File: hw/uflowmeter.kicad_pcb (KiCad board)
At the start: 4 copper layers, 70 x 55 mm, 54 parts, among them J1 SBW, J2 ANT, J3 Display, J4 Transducers, J5 Cal UART, Q1 IRLML6401, SW1 Button, U1 MSP430FR5043IRGC, U2 CC1101RGPR, Y1 32.768kHz, Y2 8MHz, Y3 26MHz

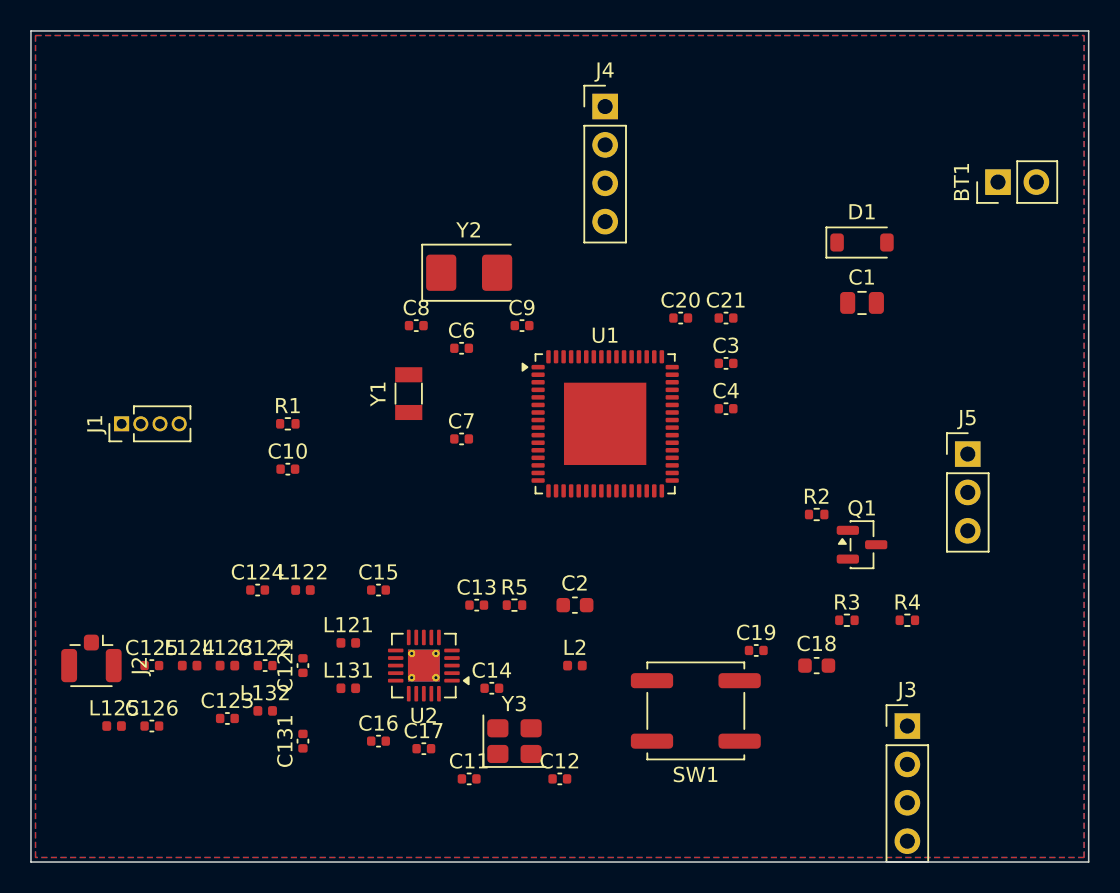
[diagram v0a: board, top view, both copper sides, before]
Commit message: hw: pour the planes and stitch the supplies, 134 unconnected down to 69
Ground and the supply rails are now carried by the planes rather than left to
routing, which is what a four-layer board is for. Filling the pours took the
unconnected count from 134 to 86; sixteen stitching vias taking VCC's surface
pads down to its plane took it to 70. DRC stays at zero violations.

The zones connect to pads solidly rather than through thermal spokes. With
relief, DRC reported starved thermals on the CC1101's ground pads -- a QFN at
0.5 mm pitch has no room for spokes -- and thermal relief under an RF ground
is the wrong thing anyway.

Signal routing is not done, and the attempt is worth recording. Straight runs
between pads were tried for the simple two-pad nets and refused themselves:
ten of eleven were blocked, because a straight line from a crystal to its QFN
pin passes over the neighbouring pins. Escaping the package and changing layer
is a router's job or a person's, not a script's.

The RF chain was excluded from that attempt on purpose. Its geometry has to be
lifted from TI's reference layout, and a generic trace between those pads
would be worse than none, because it would look finished.

Co-Authored-By: Claude Opus 5 (1M context) <noreply@anthropic.com>
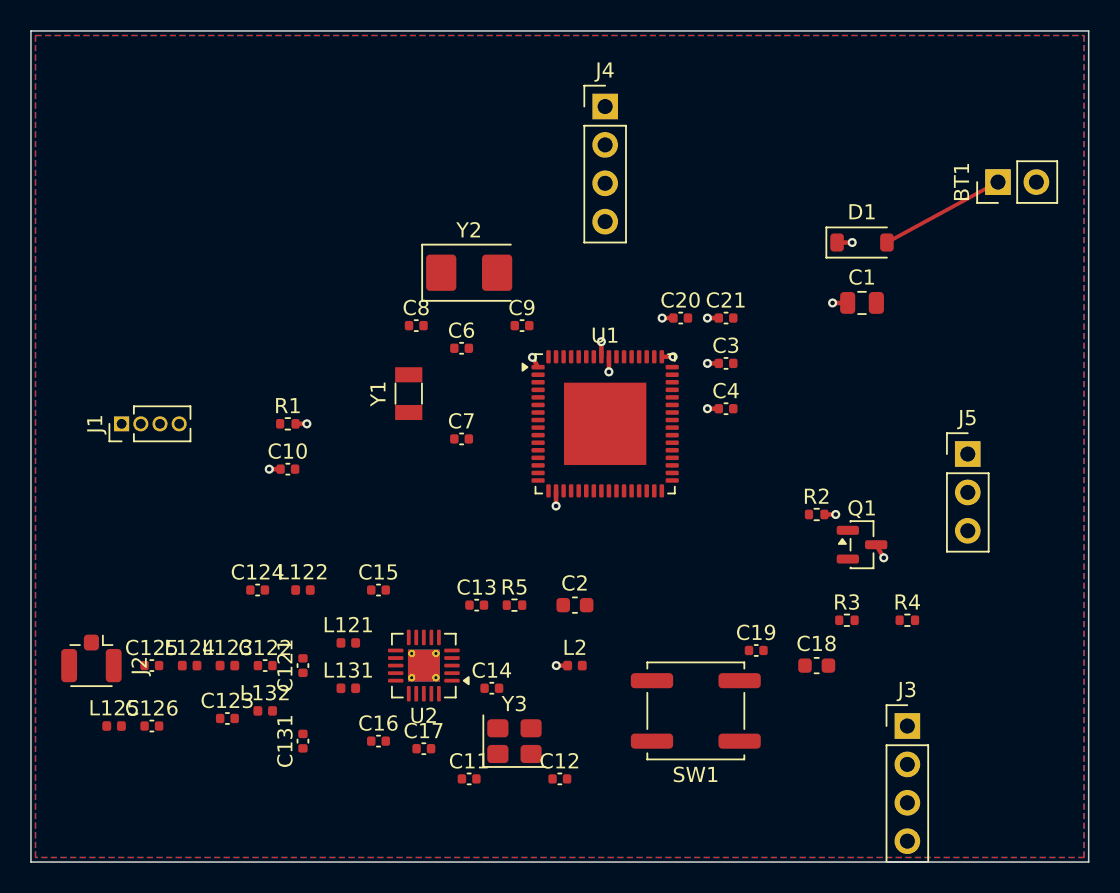
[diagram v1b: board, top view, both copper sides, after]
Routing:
- net VCC: track 0.00 -> 13.5 mm, vias 0 -> 16
- net BAT+: track 0.00 -> 8.37 mm

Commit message: hw: J3 is GND VCC SCL SDA, the way the module is actually labelled
The display header had VCC on pin 1 and ground on pin 2. The module in hand
is silkscreened GND VCC SCL SDA, so plugging it in would have put the supply
across it backwards the first time.

Both orders exist on SSD1306 breakouts, which is why this is now recorded as
having been read off the part rather than assumed -- it is worth checking
against the module in hand and not against habit.

DRC stays clean at 69 unconnected.

Co-Authored-By: Claude Opus 5 (1M context) <noreply@anthropic.com>
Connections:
- J3 pad 1: VCC_DISP -> GND
- J3 pad 2: GND -> VCC_DISP

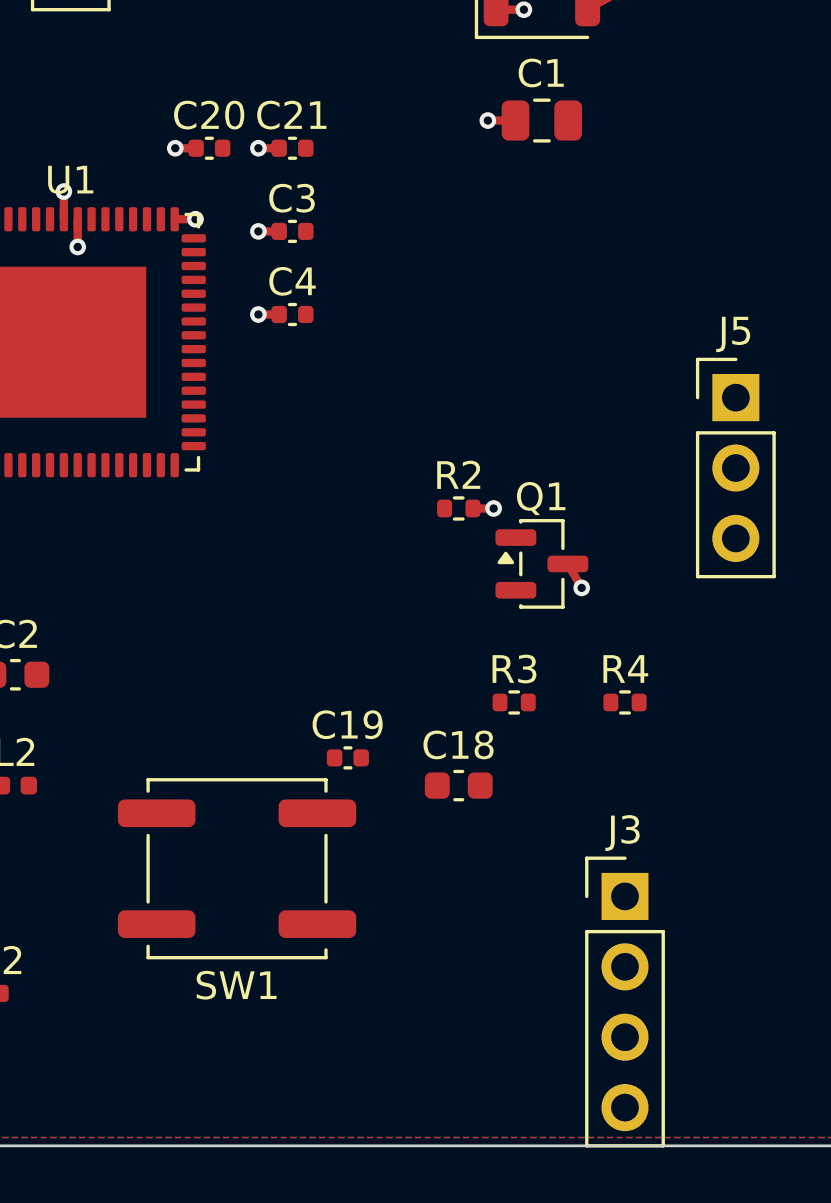
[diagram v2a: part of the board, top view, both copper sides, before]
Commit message: hw: the display mounts on the back of the board
J3 moves to the reverse side with its pins in a row rather than a column, so
the module seats directly on it facing outward instead of hanging on four
flying leads.

Where it sits was searched rather than chosen. Three constraints, and each
one rejected the position picked before it. The four drills have to miss
everything on the front -- the first attempt put them through the 8 MHz
crystal. The pin row has to run the way the module's does, or the display
reads sideways. And the 27 mm body has to clear every through-hole pin that
protrudes on that side, which J1, J4, J5 and BT1 all do; the position before
this one would have sat the module on top of the calibration header.

It also stays off the radio. A module carrying its own ground plane and a
charge pump, held a few millimetres over the 868 MHz balun, would detune the
match and inject noise into it.

Thirty-seven positions satisfy all of that. Pin 1 is at (43.5, 20.5) and the
body lands at x 33.8-60.8, y 20.5-47.5. DRC clean, 69 unconnected.

One thing to check with the part in hand: a header on the back reads mirrored
from the front, so which way round the module seats depends on which side its
body hangs.

Co-Authored-By: Claude Opus 5 (1M context) <noreply@anthropic.com>
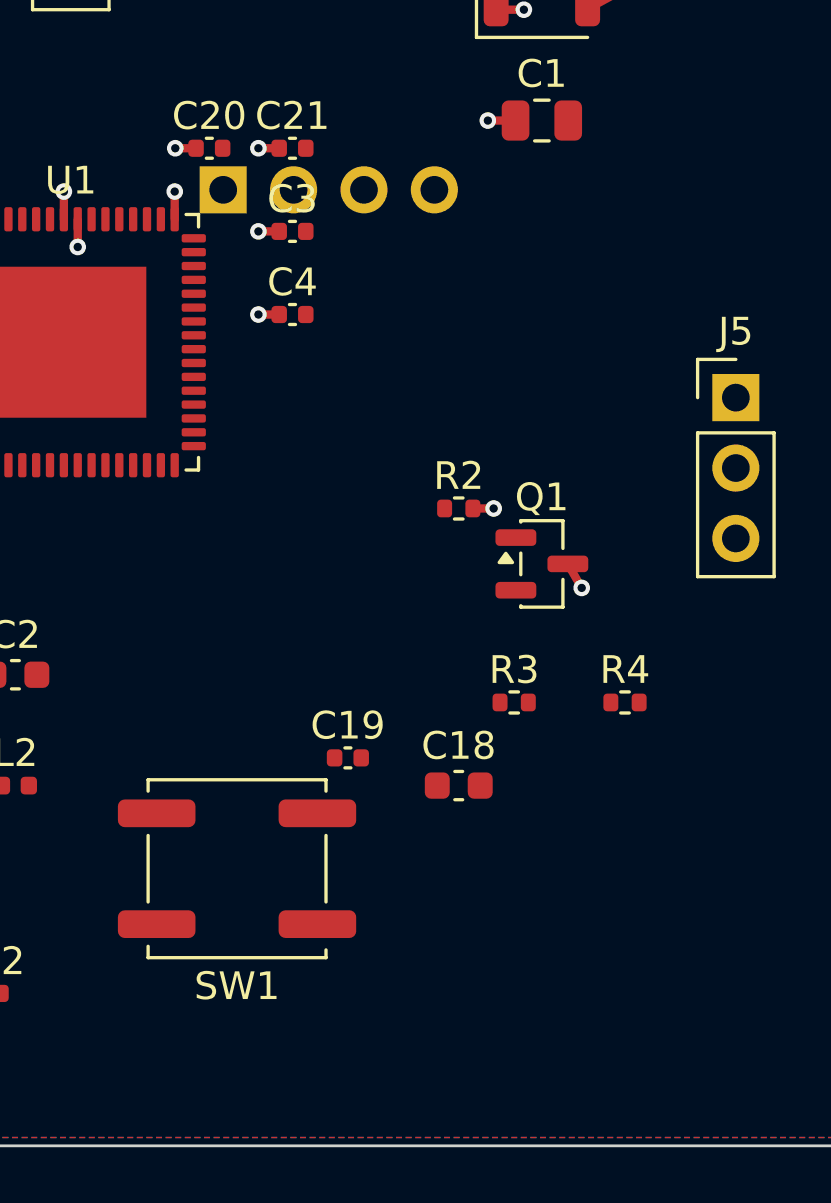
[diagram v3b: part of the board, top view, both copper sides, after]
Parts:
- J3: moved to B.Cu
- moved J3 29.3 mm to (43.5, 20.5), turned to -90 degrees

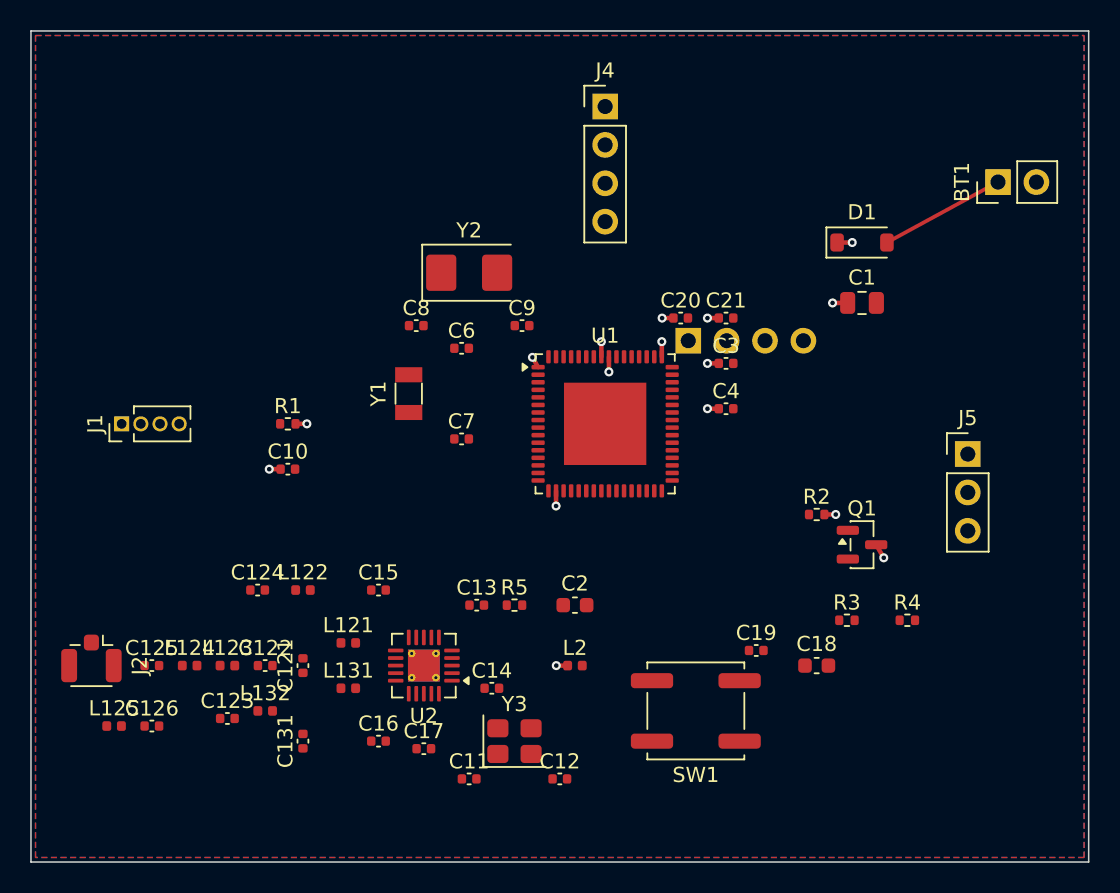
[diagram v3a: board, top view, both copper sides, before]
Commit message: hw: the right half becomes a front panel, display above the button
The display hangs from J3 at the top of the board, body over x 38.3-65.3,
y 6-33, with the button directly below it at x 47.2-56.4, y 35.9-46.1 --
three millimetres between them. Reading on top, button under it, both through
the same face of an enclosure.

This could not be done by moving the connector. A 27 mm module above the
button needs a clear column, and the search for one returned nothing: the
transducer header and the cell sat in it, and both protrude. So the board was
rearranged around the panel instead -- transducers to the top left, cell and
calibration header to the right edge below it, and the display's own passives
out from under the button.

The display also came back to the front. On the back it would have been on the
opposite face from the button, which is no use as a panel.

What remains under the module is U1 and its decoupling, all surface mount,
which the module clears on its header standoff. Fine to build and awkward to
rework: probing the MCU means lifting the display.

DRC clean at 70 unconnected.

Co-Authored-By: Claude Opus 5 (1M context) <noreply@anthropic.com>
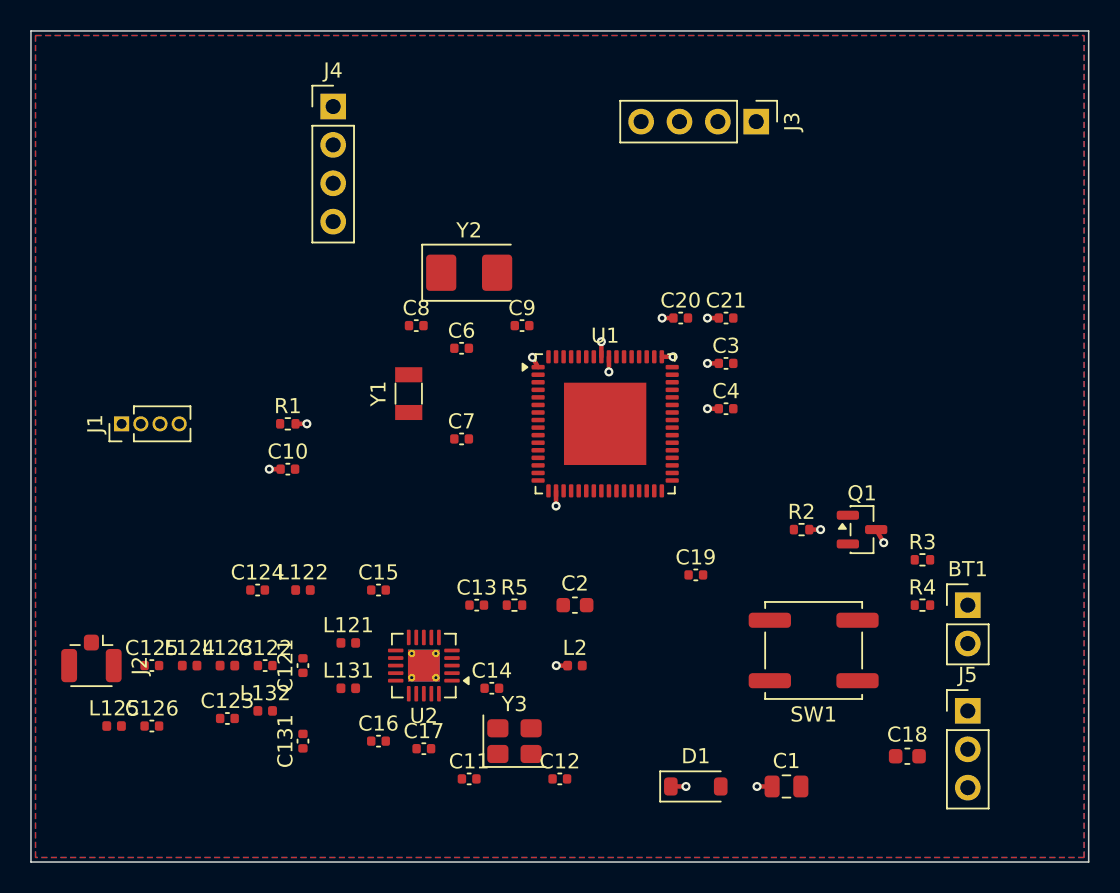
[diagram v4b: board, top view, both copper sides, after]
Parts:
- J3: moved to F.Cu
- moved D1 37.6 mm to (44.0, 50.0)
- moved C1 32.4 mm to (50.0, 50.0)
- moved BT1 28.1 mm to (62.0, 38.0), turned to 0 degrees
- moved J4 18.0 mm to (20.0, 5.00)
- moved J5 17.0 mm to (62.0, 45.0)
- moved J3 15.2 mm to (48.0, 6.00)
- moved SW1 8.77 mm to (51.8, 41.0)
- moved C18 8.49 mm to (58.0, 48.0)
- moved C19 6.40 mm to (44.0, 36.0)
- moved R3 6.40 mm to (59.0, 35.0)
- moved R2 1.41 mm to (51.0, 33.0)
- moved R4 1.41 mm to (59.0, 38.0)
- moved Q1 1.00 mm to (55.0, 33.0)
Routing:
- net BAT+: track 8.37 -> 0.00 mm

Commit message: hw: route twelve signal nets, 70 unconnected down to 36
Each pad escapes outward to a via and the run happens on the bottom layer.
That is the only thing that works on a 0.5 mm pitch QFN, where the
neighbouring pins are half a millimetre away and a straight line from a
crystal to its pin crosses three of them -- which is why the earlier attempt
routed one net out of eleven.

Three bugs stood between that and this, each worth remembering. The escape
stub was tested against the pad it started from, so no escape ever succeeded.
The bottom-layer run was tested against surface-mount pads on the top, which
it passes happily underneath -- fixing that alone took it from two nets to
eight. And the clearance used in the test was smaller than the track's own
half-width plus the class clearance, which produced six real violations
before the margin was widened.

Order matters too: routing the fattest nets first rather than alphabetically
was worth five unconnected items, since a greedy router spends whatever space
it is given.

89 tracks, 55 vias, DRC clean. What is left is fourteen signal nets the
router could not get through and the RF chain, which stays untouched on
purpose.

The routing that is there looks like machine routing -- long diagonals where
a person would go round in short hops. It is a first pass that saves the
tedious part, not a finished layout, and the USSXT pair and the I2C run in
particular are worth redoing by hand.

Co-Authored-By: Claude Opus 5 (1M context) <noreply@anthropic.com>
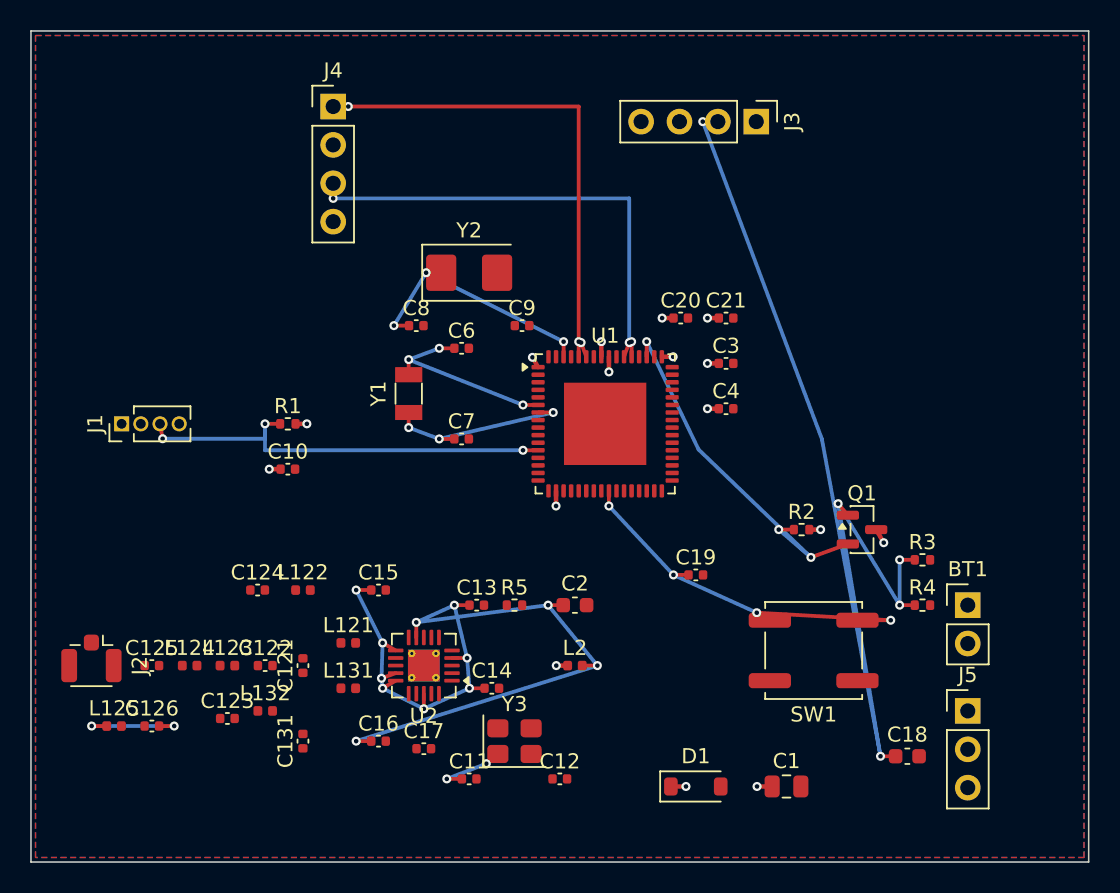
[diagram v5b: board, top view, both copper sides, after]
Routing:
- net VCC_DISP: track 0.00 -> 76.6 mm, vias 0 -> 5
- net RADIO_VDD: track 0.00 -> 64.3 mm, vias 0 -> 12
- net CH0: track 0.00 -> 34.0 mm, vias 0 -> 3
- net CH1: track 0.00 -> 32.3 mm, vias 0 -> 3
- net RST: track 0.00 -> 29.6 mm, vias 0 -> 3
- net BUTTON: track 0.00 -> 26.4 mm, vias 0 -> 4
- net DISP_GATE: track 0.00 -> 25.6 mm, vias 0 -> 3
- net USSXTIN: track 0.00 -> 17.3 mm, vias 0 -> 3
- net LFXIN: track 0.00 -> 13.3 mm, vias 0 -> 3
- net LFXOUT: track 0.00 -> 12.9 mm, vias 0 -> 3
- net RFNOTCH: track 0.00 -> 7.47 mm, vias 0 -> 2
- net XOSC_Q1: track 0.00 -> 4.80 mm, vias 0 -> 2
